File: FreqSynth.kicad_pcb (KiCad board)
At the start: 4 copper layers, 79 x 50 mm, 118 parts, among them IC1 ATMEGA32U2, P1 CPL-CON-BARREL-2.1MM, P10 RESET, P2 RF1, P3 RF2P, P4 RF2N, P5 USB_MINI_B, P6 CONN_01X06, P7 REF_IN, P8 VTEST, P9 PWRSEL, U1 MAX2870, U2 TS5A3159, U5 CPL-REG-LIN-3.3V-0.15A, U6 SKY13322-375LF, U7 SKY13322-375LF, U8 TRF37A75, U9 PE43711, X1 25MHz ±5ppm 3.3V 33mA, X2 8MHz 18PF 50ppm

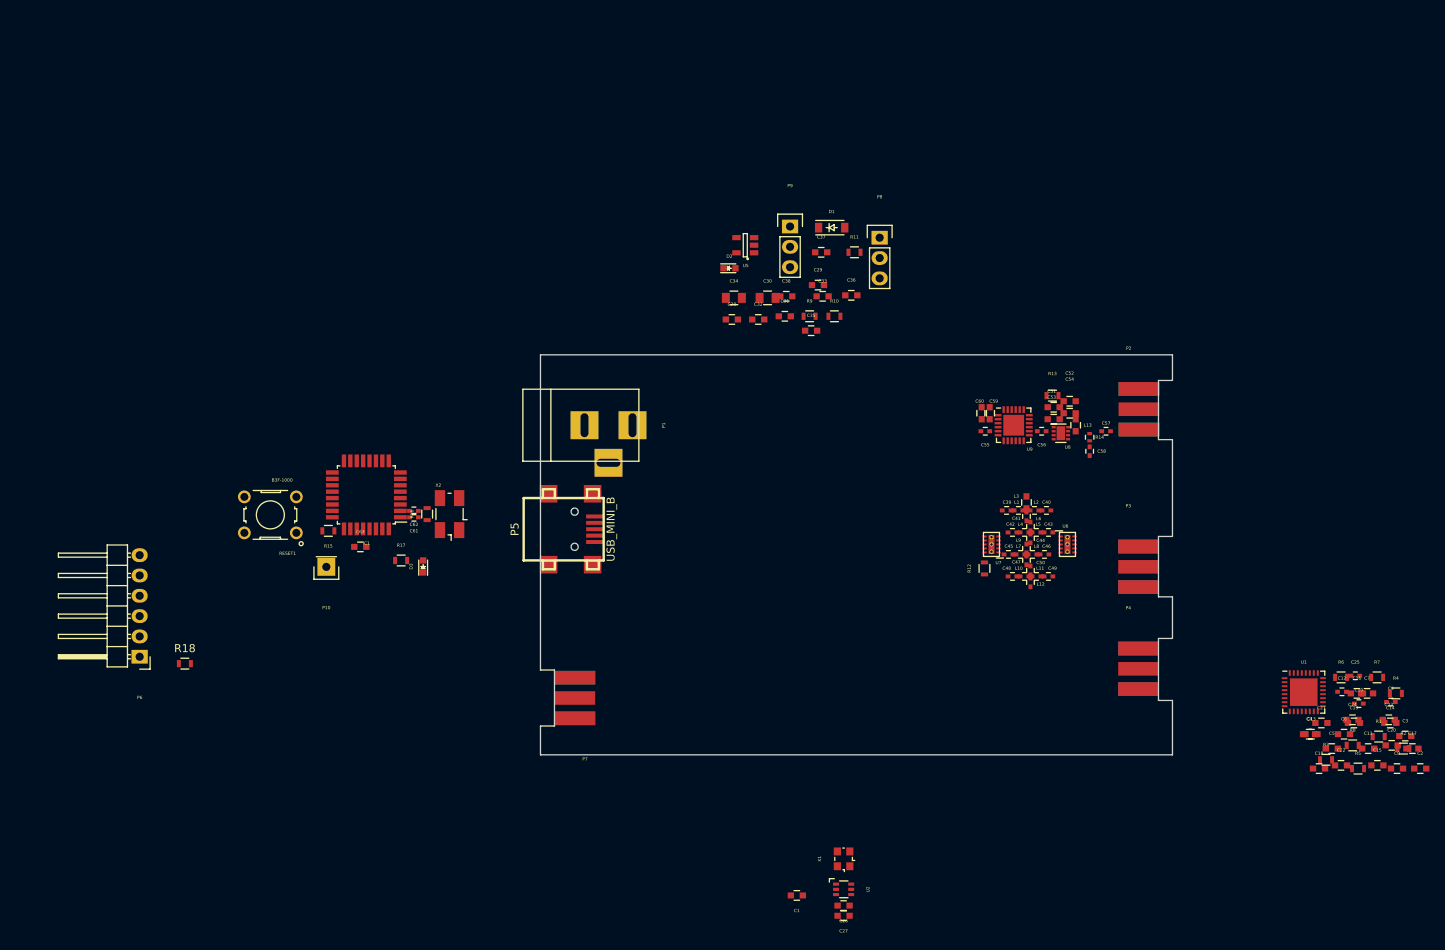
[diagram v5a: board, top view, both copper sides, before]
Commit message: Added power meter, swaped some pins, and routetd most of the RF
Signed-off-by: Martin Berglund <LeastSignificantBit@users.noreply.github.com>
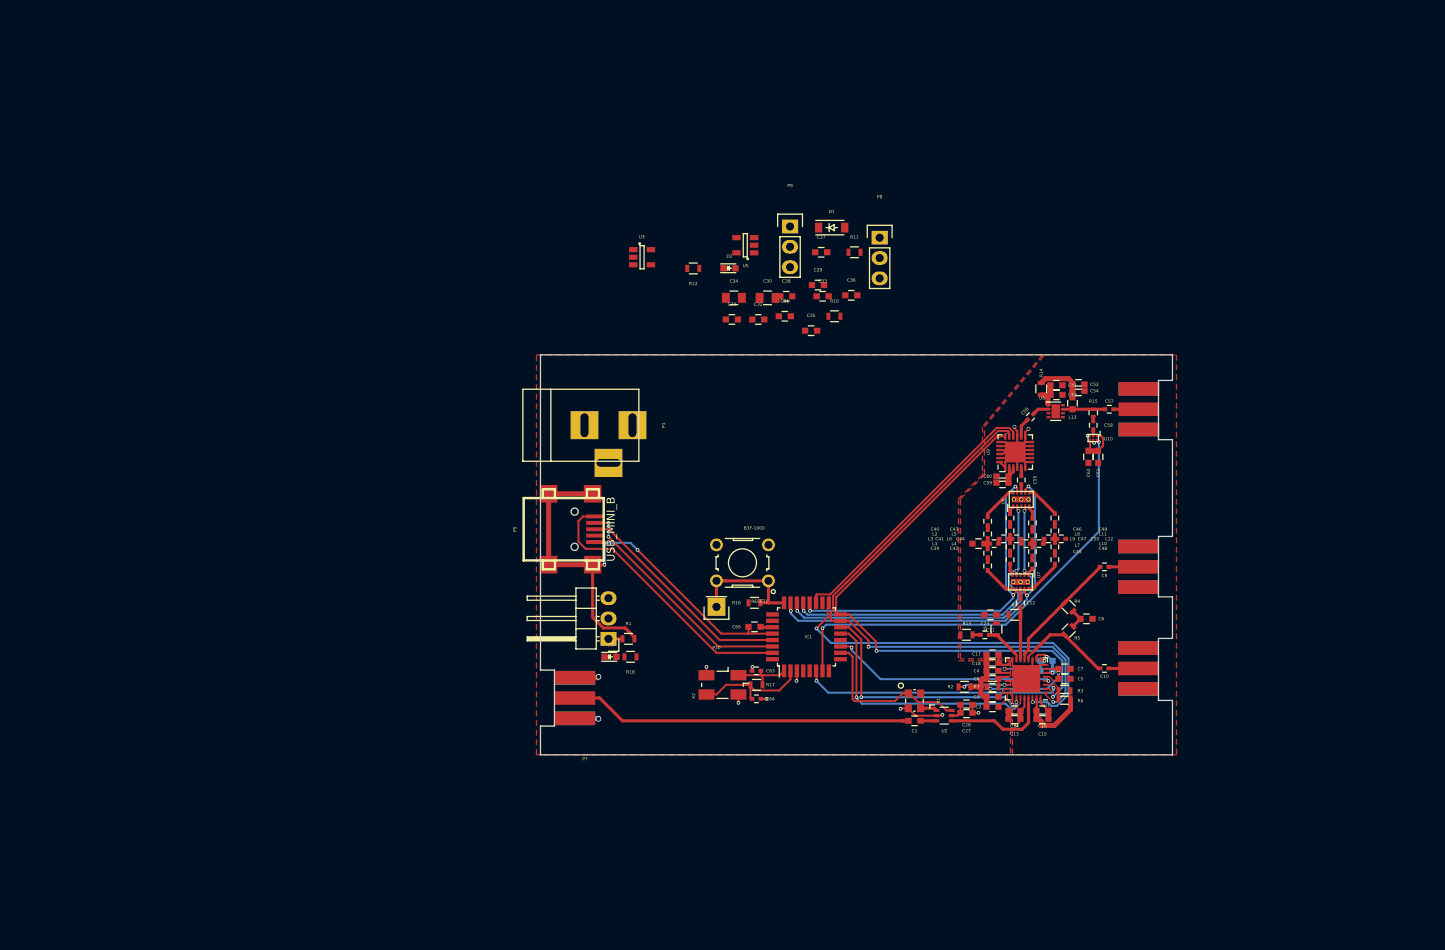
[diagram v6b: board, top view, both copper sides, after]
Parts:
- removed the C19 at (202.2, 146.0)
- removed C22, C24: 100pF, Capacitors_SMD:C_0603
- removed the C23 at (206.5, 145.6)
- added C64: 22p, Capacitors_SMD:C_0402, F.Cu at (127.5, 143.0)
- added C65: 1µF, Capacitors_SMD:C_0603, F.Cu at (127.2, 134.0)
- added U10: LMH2110, FreqSynth:WFBGA-6, F.Cu at (169.6, 110.4)
- added U3: CPL-REG-LIN-3.3V-1A, TO_SOT_Packages_SMD:SOT-23-5, F.Cu at (113.2, 87.8)
- C19: renamed from C21; moved to B.Cu
- C20: moved to B.Cu
- C61: value 22p -> 10nF; footprint Capacitors_SMD:C_0402 -> Capacitors_SMD:C_0603
- C62: value 22p -> 100pF; footprint Capacitors_SMD:C_0402 -> Capacitors_SMD:C_0603
- C63: value 1µF -> 22p; footprint Capacitors_SMD:C_0603 -> Capacitors_SMD:C_0402
- P6: value CONN_01X06 -> CONN_01X03; footprint Pin_Headers:Pin_Header_Angled_1x06 -> Pin_Headers:Pin_Header_Angled_1x03
- R1: value 5.1k -> 0R
- R11: value 33R -> 0R
- R12: value 49.9R -> 33R
- R13: value 1.8R -> 49.9R
- R14: value 100R -> 1.8R; footprint Resistors_SMD:R_0402 -> Resistors_SMD:R_0603
- R15: value 10k -> 100R; footprint Resistors_SMD:R_0603 -> Resistors_SMD:R_0402
- R16: value 1M -> 10k
- R17: value 33R -> 1M
- R18: value 0R -> 33R
- R2: value 30.1R -> 5.1k
- R3: value 49.9R -> 30.1R
- R5: value 90.9R -> 49.9R
- R6: value 240R -> 90.9R
- R7: value 49.9R -> 240R
- R9: value 0R -> 49.9R
- X1: footprint Crystals:Crystal_SMD_2520_4Pads -> FreqSynth:OSC_2.7x2.4mm
- moved R15 96.7 mm to (169.6, 107.2), turned to 270 degrees
- moved R1 94.6 mm to (111.5, 135.5)
- moved C61 85.8 mm to (170.2, 112.8), turned to 270 degrees
- moved C62 84.6 mm to (169.0, 112.8), turned to 270 degrees
- moved RESET1 59.3 mm to (125.8, 126.0)
- moved P6 58.6 mm to (109.0, 135.5)
- moved IC1 57.8 mm to (133.8, 135.2), turned to 90 degrees
- moved R18 55.7 mm to (111.8, 137.8), turned to 180 degrees
- moved R2 55.4 mm to (153.5, 141.5), turned to 180 degrees
- moved C2 54.0 mm to (157.0, 144.0)
- moved C17 53.8 mm to (157.0, 137.5), turned to 180 degrees
- moved R12 52.3 mm to (119.6, 89.2), turned to 180 degrees
- moved C63 51.9 mm to (127.5, 139.5)
- moved C3 51.8 mm to (157.0, 142.8)
- moved C8 51.8 mm to (157.0, 140.5)
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- renumbered C25 to C23
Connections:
- C10 pad 1: /PLL/RF_BALANCED- -> /PLL/RF_BALANCED+
- C10 pad 2: /PLL/RFB_N -> /PLL/RFA_P
- C11 pad 1: /Amplifier/VCC_AMP -> /Amplifier/3V3
- C12 pad 2: /PLL/RFA_P -> /PLL/RFB_P
- C17 pad 1: /Amplifier/VCC_AMP -> /Amplifier/3V3
- C18 pad 1: /Amplifier/VCC_AMP -> /Amplifier/3V3
- C20 pad 1: /Amplifier/VCC_AMP -> /PLL/VCC_PLL
- C20 pad 2: Earth -> GNDD
- C23 pad 2: /PLL/RFA_N -> /PLL/RFB_N
- C32 pad 1: /Amplifier/VCC_AMP -> /Amplifier/3V3
- C33 pad 1: /Amplifier/VCC_AMP -> /Amplifier/3V3
- C51 pad 2: /Amplifier/VCC_AMP -> /Amplifier/3V3
- C53 pad 2: /Amplifier/VCC_AMP -> /Amplifier/3V3
- C6 pad 1: /Amplifier/VCC_AMP -> /Amplifier/3V3
- C61 pad 1: GNDD -> /Amplifier/3V3
- C61 pad 2: Net-(C61-Pad2) -> Earth
- C62 pad 1: GNDD -> /Amplifier/3V3
- C62 pad 2: Net-(C62-Pad2) -> Earth
- C63 pad 1: Net-(C63-Pad1) -> GNDD
- C63 pad 2: GNDPWR -> Net-(C63-Pad2)
- C9 pad 1: /PLL/RF_BALANCED+ -> /PLL/RF_BALANCED-
- C9 pad 2: /PLL/RFB_P -> /PLL/RFA_N
- IC1 pad 1: Net-(C61-Pad2) -> Net-(C63-Pad2)
- IC1 pad 10: /FILT1 -> /MCU/EXT_CLK_EN
- IC1 pad 11: /FILT2 -> /MCU/CE_PLL
- IC1 pad 12: /FILT3 -> Net-(IC1-Pad12)
- IC1 pad 13: /FILT4 -> /MCU/EN_PLL
- IC1 pad 14: /MCU/SS_EXT -> /MCU/LD_PLL
- IC1 pad 19: Net-(IC1-Pad19) -> /Amplifier/ATTEN_CS
- IC1 pad 2: Net-(C62-Pad2) -> Net-(C64-Pad2)
- IC1 pad 20: Net-(IC1-Pad20) -> /FILT1
- IC1 pad 21: Net-(IC1-Pad21) -> /FILT4
- IC1 pad 22: Net-(D3-Pad1) -> /FILT3
- IC1 pad 23: /MCU/EXT_CLK_EN -> /FILT2
- IC1 pad 26: /Amplifier/ATTEN_CS -> Net-(IC1-Pad26)
- IC1 pad 27: Net-(C63-Pad1) -> Net-(C65-Pad1)
- IC1 pad 5: Net-(IC1-Pad5) -> Net-(D3-Pad1)
- IC1 pad 7: /MCU/CE_PLL -> /MCU/ADC1
- IC1 pad 8: /MCU/LD_PLL -> /MCU/TX
- IC1 pad 9: /MCU/EN_PLL -> /MCU/RX
- P6 pad 2: Net-(P6-Pad2) -> /MCU/RX
- P6 pad 3: Net-(P6-Pad3) -> /MCU/TX
- P8 pad 2: /Amplifier/VCC_AMP -> /Amplifier/3V3
- R1 pad 1: Earth -> Net-(P6-Pad1)
- R1 pad 2: Net-(R1-Pad2) -> GNDPWR
- R10 pad 1: Earth -> GNDD
- R11 pad 1: VCC -> Earth
- R11 pad 2: Net-(D2-Pad2) -> GNDPWR
- R12 pad 1: /PLL/RF- -> VCC
- R12 pad 2: Earth -> Net-(D2-Pad2)
- R13 pad 1: /Amplifier/VCC_AMP -> /PLL/RF-
- R13 pad 2: Net-(C52-Pad1) -> Earth
- R14 pad 1: Net-(C57-Pad2) -> /Amplifier/3V3
- R14 pad 2: Net-(C58-Pad2) -> Net-(C52-Pad1)
- R15 pad 1: VCC -> Net-(C57-Pad2)
- R15 pad 2: Net-(IC1-Pad24) -> Net-(C58-Pad2)
- R16 pad 1: Net-(C61-Pad2) -> VCC
- R16 pad 2: Net-(C62-Pad2) -> Net-(IC1-Pad24)
- R17 pad 1: VCC -> Net-(C63-Pad2)
- R17 pad 2: Net-(D3-Pad2) -> Net-(C64-Pad2)
- R18 pad 1: Net-(P6-Pad1) -> VCC
- R18 pad 2: GNDPWR -> Net-(D3-Pad2)
- R2 pad 1: Net-(C5-Pad2) -> Earth
- R3 pad 1: /Amplifier/VCC_AMP -> Net-(C5-Pad2)
- R3 pad 2: /PLL/RFB_P -> Net-(R3-Pad2)
- R4 pad 1: /Amplifier/VCC_AMP -> /Amplifier/3V3
- R4 pad 2: /PLL/RFB_N -> /PLL/RFA_N
- R5 pad 1: GNDD -> /Amplifier/3V3
- R5 pad 2: Net-(R2-Pad2) -> /PLL/RFA_P
- R6 pad 1: /PLL/TUNE -> GNDD
- R6 pad 2: Net-(C5-Pad1) -> Net-(R3-Pad2)
- R7 pad 1: /Amplifier/VCC_AMP -> /PLL/TUNE
- R7 pad 2: /PLL/RFA_P -> Net-(C5-Pad1)
- R8 pad 1: /Amplifier/VCC_AMP -> /Amplifier/3V3
- R8 pad 2: /PLL/RFA_N -> /PLL/RFB_P
- R9 pad 1: GNDD -> /Amplifier/3V3
- R9 pad 2: GNDPWR -> /PLL/RFB_N
- U1 pad 16: /Amplifier/VCC_AMP -> /Amplifier/3V3
- U1 pad 17: /Amplifier/VCC_AMP -> /Amplifier/3V3
- U1 pad 22: Net-(R1-Pad2) -> Net-(R2-Pad2)
- U1 pad 5: Net-(R2-Pad2) -> Net-(R3-Pad2)
- U8 pad 1: /Amplifier/VCC_AMP -> /Amplifier/3V3
- X2 pad 1: Net-(C61-Pad2) -> Net-(C63-Pad2)
- X2 pad 2: Net-(C62-Pad2) -> Net-(C64-Pad2)
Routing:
- net /SCK: track 0.00 -> 73.8 mm, vias 0 -> 2
- net /MOSI: track 0.00 -> 69.6 mm, vias 0 -> 2
- net GNDPWR: track 0.00 -> 64.9 mm, vias 0 -> 3
- net /MCU/ADC1: track 0.00 -> 56.5 mm, vias 0 -> 2
- net /FILT2: track 0.00 -> 49.2 mm, vias 0 -> 3
- net /MISO: track 0.00 -> 47.2 mm, vias 0 -> 2
- net /FILT3: track 0.00 -> 43.8 mm, vias 0 -> 3
- net /FILT1: track 0.00 -> 43.7 mm, vias 0 -> 3
- net Net-(C1-Pad2): track 0.00 -> 43.7 mm
- net /FILT4: track 0.00 -> 42.2 mm, vias 0 -> 3
- net Earth: track 0.00 -> 42.2 mm, vias 0 -> 4
- net GNDD: track 0.00 -> 38.4 mm, vias 0 -> 12
- net /Amplifier/ATTEN_CS: track 0.00 -> 35.0 mm
- net /Power/VUSB: track 0.00 -> 34.9 mm
- net /MCU/CS_PLL: track 0.00 -> 33.1 mm, vias 0 -> 2
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- added copper zone on F.Cu, net Earth
- added copper zone on In1.Cu, net Earth
- added copper zone on F.Cu, net GNDD
- added copper zone on In1.Cu, net GNDD
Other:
- net class 50Ohm added: clearance 0.127, trace_width 0.3937, via_dia 0.4572, via_drill 0.254

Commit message: Starting to clean up
Signed-off-by: Martin Berglund <LeastSignificantBit@users.noreply.github.com>
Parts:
- removed the C31 at (131.0, 95.2)
- removed the P8 at (142.9, 85.4)
- removed P9: PWRSEL, Pin_Headers:Pin_Header_Straight_1x03
- added C28: 1µF, Capacitors_SMD:C_0603, F.Cu at (92.8, 78.9)
- added C29: 100nF, Capacitors_SMD:C_0603, F.Cu at (88.6, 78.9)
- added C63: 10nF, Capacitors_SMD:C_0603, F.Cu at (134.5, 142.5)
- added C64: 100pF, Capacitors_SMD:C_0603, F.Cu at (133.0, 142.5)
- added TH1: 750mA working 1.5A trip, FreqSynth:SMD_THERMISTOR, F.Cu at (117.7, 106.2)
- added U5: CPL-REG-LIN-3.3V-0.15A, TO_SOT_Packages_SMD:SOT-23-5, F.Cu at (96.5, 72.7)
- C30: value 10µF -> 10nF; footprint Capacitors_SMD:C_0805 -> Capacitors_SMD:C_0603
- moved C30 35.3 mm to (96.4, 78.9)
- renumbered C23 to C21, C26 to C22, C27 to C23, C28 to C24, C29 to C25, C32 to C26, C33 to C27, C34 to C31, C35 to C32, C36 to C33, C37 to C34, C38 to C35, C39 to C36, C40 to C37, C41 to C38, C42 to C39, C43 to C40, C44 to C41, C45 to C42, C46 to C43, C47 to C44, C48 to C45, C49 to C46, C50 to C47, C51 to C48, C52 to C49, C53 to C50, C54 to C51, C55 to C52, C56 to C53, C57 to C54, C58 to C55, C59 to C56, C60 to C57, C61 to C58, C62 to C59, C63 to C60, C64 to C61, C65 to C62, P10 to P8, R12 to R10, R10 to R11, R11 to R12, R18 to R17, R17 to R18, U9 to U10, U10 to U11, U5 to U6, U6 to U7, U7 to U8, U8 to U9
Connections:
- C11 pad 1: /Amplifier/3V3 -> /PLL/VCC_RF
- C13 pad 1: VCC -> /MCU/VCC_D
- C14 pad 1: VCC -> /MCU/VCC_D
- C15 pad 1: VCC -> /MCU/VCC_D
- C16 pad 1: VCC -> /MCU/VCC_D
- C17 pad 1: /Amplifier/3V3 -> /PLL/VCC_RF
- C18 pad 1: /Amplifier/3V3 -> /PLL/VCC_RF
- C22 pad 1: VCC -> /3v3
- C23 pad 1: VCC -> /3v3
- C24 pad 1: VCC -> /MCU/VCC_D
- C25 pad 1: VCC -> /MCU/VCC_D
- C26 pad 1: /Amplifier/3V3 -> /PLL/VCC_RF
- C26 pad 2: Earth -> Net-(C26-Pad2)
- C27 pad 1: /Amplifier/3V3 -> /PLL/VCC_RF
- C27 pad 2: Earth -> Net-(C26-Pad2)
- C30 pad 1: /Power/VUSB -> Net-(C30-Pad1)
- C30 pad 2: GNDPWR -> GNDD
- C48 pad 2: /Amplifier/3V3 -> /5V5
- C50 pad 2: /Amplifier/3V3 -> /5V5
- C56 pad 1: /Amplifier/3V3 -> /3v3
- C57 pad 1: /Amplifier/3V3 -> /3v3
- C58 pad 1: /Amplifier/3V3 -> /3v3
- C59 pad 1: /Amplifier/3V3 -> /3v3
- C6 pad 1: /Amplifier/3V3 -> /PLL/VCC_RF
- IC1 pad 31: /Power/VUSB -> /MCU/V_USB
- IC1 pad 32: VCC -> /MCU/VCC_D
- IC1 pad 4: VCC -> /MCU/VCC_D
- P1 pad 1: /Power/VIN -> Net-(P1-Pad1)
- P5 pad 1: /Power/VUSB -> /MCU/V_USB
- R10 pad 1: VCC -> /MCU/VCC_D
- R14 pad 1: /Amplifier/3V3 -> /5V5
- R16 pad 1: VCC -> /MCU/VCC_D
- R17 pad 1: VCC -> /MCU/VCC_D
- R4 pad 1: /Amplifier/3V3 -> /PLL/VCC_RF
- R5 pad 1: /Amplifier/3V3 -> /PLL/VCC_RF
- R8 pad 1: /Amplifier/3V3 -> /PLL/VCC_RF
- R9 pad 1: /Amplifier/3V3 -> /PLL/VCC_RF
- U1 pad 16: /Amplifier/3V3 -> /PLL/VCC_RF
- U1 pad 17: /Amplifier/3V3 -> /PLL/VCC_RF
- U1 pad 28: VCC -> /MCU/VCC_D
- U1 pad 32: VCC -> /MCU/VCC_D
- U10 pad 2: /Amplifier/3V3 -> /3v3
- U10 pad 3: /Amplifier/3V3 -> /3v3
- U11 pad A1: /Amplifier/3V3 -> /3v3
- U11 pad C2: /Amplifier/3V3 -> /3v3
- U2 pad 5: VCC -> /3v3
- U3 pad 1: Net-(P9-Pad2) -> /Power/VIN
- U3 pad 3: VCC -> /MCU/VCC_D
- U6 pad 1: Net-(P9-Pad2) -> Net-(U6-Pad1)
- U6 pad 3: Net-(P9-Pad2) -> Net-(U6-Pad1)
- U9 pad 1: /Amplifier/3V3 -> /5V5
- X1 pad 4: VCC -> /3v3
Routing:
- net /MCU/VCC_D: track 0.00 -> 50.7 mm, vias 0 -> 5
- net /Power/VUSB: track 34.9 -> 0.00 mm
- net /MCU/V_USB: track 0.00 -> 34.9 mm
- net /MCU/RX: track 0.00 -> 32.3 mm, vias 0 -> 2
- net /MCU/TX: track 0.00 -> 31.9 mm, vias 0 -> 2
- net /Amplifier/3V3: track 18.2 -> 0.00 mm
- net /3v3: track 0.00 -> 11.1 mm
- net VCC: track 9.02 -> 0.00 mm, vias 1 -> 0
- net /PLL/VCC_RF: track 0.00 -> 5.78 mm
- net /5V5: track 0.00 -> 3.64 mm

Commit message: Board layout almost done
Signed-off-by: Martin Berglund <LeastSignificantBit@users.noreply.github.com>
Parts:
- removed the C26 at (127.7, 95.6)
- removed the D2 at (124.1, 89.2)
- added ?: , FreqSynth:VIA, F.Cu at (161.0, 121.6)
- added C25: 22µF 16V, Capacitors_SMD:C_0805, F.Cu at (118.8, 111.5)
- added C32: 1µF, Capacitors_SMD:C_0603, F.Cu at (110.5, 116.8)
- added D3: CPL-LED-0603-GREEN, LEDs:LED_0603, F.Cu at (104.0, 128.5)
- added L1: Ferrite, FreqSynth:L_0603, F.Cu at (161.0, 104.5)
- added L2: Ferrite, FreqSynth:L_0603, F.Cu at (157.0, 145.5)
- added L3: Ferrite, FreqSynth:L_0603, F.Cu at (167.8, 112.8)
- added L4: Ferrite, FreqSynth:L_0603, F.Cu at (156.8, 131.5)
- added L5: Ferrite, FreqSynth:L_0603, F.Cu at (165.4, 138.2)
- added L6: Ferrite, FreqSynth:L_0603, F.Cu at (137.0, 141.5)
- added L7: Ferrite, FreqSynth:L_0603, F.Cu at (145.5, 140.0)
- added L8: 6.8µH 2.5A, FreqSynth:NRS5030T6R8MMGJ, F.Cu at (114.0, 117.5)
- added R13: 11.3k, Resistors_SMD:R_0603, F.Cu at (124.8, 116.8)
- added R20: 33R, Resistors_SMD:R_0603, F.Cu at (110.5, 138.0)
- added SG1: StarGND, FreqSynth:NetTie-II_Connected_SMD, B.Cu at (121.2, 112.8)
- added U4: AP65101, TO_SOT_Packages_SMD:SOT-23-6, F.Cu at (118.5, 116.8)
- C27, C29, C34: value 100nF -> 1µF
- C30, C35: value 10nF -> 1µF
- C31: value 10µF -> 1µF; footprint Capacitors_SMD:C_0805 -> Capacitors_SMD:C_0603
- C33: value 1µF -> 22µF 16V; footprint Capacitors_SMD:C_0603 -> Capacitors_SMD:C_0805
- R10: value 33R -> 45.3k
- R11: value 0R -> 59k
- R12: value 0R -> 100k
- U3: value CPL-REG-LIN-3.3V-1A -> TLV7113333DDSET; footprint TO_SOT_Packages_SMD:SOT-23-5 -> FreqSynth:WSON-6
- U5: value CPL-REG-LIN-3.3V-0.15A -> TLV7113333DDSET; footprint TO_SOT_Packages_SMD:SOT-23-5 -> FreqSynth:WSON-6
- U6: value CPL-REG-LIN-3.3V-0.15A -> RT9069-50GB
- U9: footprint Housings_DFN_QFN:DFN-8-1EP_2x2mm_Pitch0.5mm -> FreqSynth:DFN-8-1EP_2x2mm_Pitch0.5mm
- moved C28 63.5 mm to (138.0, 123.5), turned to 270 degrees
- moved C29 61.6 mm to (138.0, 115.8), turned to 270 degrees
- moved U5 59.6 mm to (136.2, 117.2), turned to 270 degrees
- moved C30 52.8 mm to (134.2, 115.8), turned to 90 degrees
- moved U3 41.7 mm to (136.2, 122.5), turned to 270 degrees
- moved C34 36.7 mm to (119.8, 120.2), turned to 270 degrees
- moved C33 35.2 mm to (118.0, 120.5), turned to 270 degrees
- moved R12 34.9 mm to (121.2, 116.8), turned to 270 degrees
- moved D1 31.6 mm to (118.1, 109.5), turned to 180 degrees
- moved R10 31.1 mm to (121.2, 120.2), turned to 90 degrees
- moved C24 28.8 mm to (138.0, 121.0), turned to 270 degrees
- moved C31 28.7 mm to (138.0, 118.2), turned to 270 degrees
- moved C27 28.4 mm to (134.2, 121.0), turned to 90 degrees
- moved R11 25.8 mm to (123.0, 116.8), turned to 90 degrees
- moved C26 22.5 mm to (118.8, 113.2), turned to 180 degrees
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- renumbered C32 to C26, C25 to C36, C36 to C37, C37 to C38, C38 to C39, C39 to C40, C40 to C41, C41 to C42, C42 to C43, C43 to C44, C44 to C45, C45 to C46, C46 to C47, C47 to C48, C48 to C49, C49 to C50, C50 to C51, C51 to C52, C52 to C53, C53 to C54, C54 to C55, C55 to C56, C56 to C57, C57 to C58, C58 to C59, C59 to C60, C60 to C61, C61 to C62, C62 to C63, C63 to C64, C64 to C65, D3 to D2, L2 to L10, L3 to L11, L4 to L12, L5 to L13, L6 to L14, L7 to L15, L8 to L16, L9 to L17, L10 to L18, L11 to L19, L12 to L20, L13 to L21, L1 to L9, R13 to R14, R14 to R15, R15 to R16, R16 to R17, R17 to R18, R18 to R19
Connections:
- C13 pad 1: /MCU/VCC_D -> /PLL/VCC_D
- C14 pad 1: /MCU/VCC_D -> /PLL/VCC_D
- C15 pad 1: /MCU/VCC_D -> /PLL/VCC_D
- C16 pad 1: /MCU/VCC_D -> /PLL/VCC_D
- C22 pad 1: /3v3 -> /Clock/3V3
- C23 pad 1: /3v3 -> /Clock/3V3
- C24 pad 1: /MCU/VCC_D -> GNDD
- C24 pad 2: GNDD -> /Power/VCC_D
- C27 pad 1: /PLL/VCC_RF -> /Power/4V0
- C27 pad 2: Net-(C26-Pad2) -> GNDD
- C28 pad 1: /3v3 -> /Power/VCC_PLL
- C28 pad 2: GNDD -> Earth
- C29 pad 1: /3v3 -> Earth
- C29 pad 2: GNDD -> /3v3
- C30 pad 1: Net-(C30-Pad1) -> /Power/4V0
- C30 pad 2: GNDD -> Earth
- C31 pad 1: /Power/VIN -> /Power/VCC_RF
- C31 pad 2: GNDPWR -> Earth
- C33 pad 1: /PLL/VCC_PLL -> /Power/4V0
- C33 pad 2: GNDD -> GNDPWR
- C34 pad 1: /PLL/VCC_PLL -> /Power/4V0
- C34 pad 2: GNDD -> GNDPWR
- C35 pad 1: Net-(C35-Pad1) -> /5V5
- C35 pad 2: GNDD -> Earth
- C36 pad 1: /MCU/VCC_D -> /Power/VIN
- C36 pad 2: GNDD -> Earth
- C49 pad 2: /5V5 -> /Amplifier/VCC_AMP
- C51 pad 2: /5V5 -> /Amplifier/VCC_AMP
- C57 pad 1: /3v3 -> /Amplifier/3V3
- C58 pad 1: /3v3 -> /Amplifier/3V3
- C59 pad 1: /3v3 -> /Amplifier/3V3
- C60 pad 1: /3v3 -> /Amplifier/3V3
- R10 pad 1: /MCU/VCC_D -> Net-(R10-Pad1)
- R10 pad 2: Net-(D2-Pad2) (its old number) -> /Power/4V0
- R11 pad 1: GNDD -> Net-(R10-Pad1)
- R11 pad 2: GNDPWR -> Net-(R11-Pad2)
- R12 pad 1: Earth -> /Power/VIN
- R12 pad 2: GNDPWR -> Net-(R12-Pad2)
- R15 pad 1: /5V5 -> /Amplifier/VCC_AMP
- U1 pad 28: /MCU/VCC_D -> /PLL/VCC_D
- U1 pad 32: /MCU/VCC_D -> /PLL/VCC_D
- U10 pad 2: /3v3 -> /Amplifier/3V3
- U10 pad 3: /3v3 -> /Amplifier/3V3
- U11 pad A1: /3v3 -> /Amplifier/3V3
- U11 pad C2: /3v3 -> /Amplifier/3V3
- U2 pad 5: /3v3 -> /Clock/3V3
- U3 pad 1: /Power/VIN -> /Power/4V0
- U3 pad 2: GNDD -> /Power/4V0
- U3 pad 3: /MCU/VCC_D -> /Power/4V0
- U3 pad 4: (no net) -> GNDD
- U3 pad 5: (no net) -> /Power/VCC_PLL
- U5 pad 1: /Power/VIN -> /Power/4V0
- U5 pad 2: GNDD -> /Power/4V0
- U5 pad 3: /Power/VIN -> /Power/4V0
- U5 pad 4: Net-(C30-Pad1) -> Earth
- U5 pad 5: /3v3 -> /Power/VCC_RF
- U6 pad 1: Net-(U6-Pad1) -> /Power/VIN
- U6 pad 2: GNDD -> Earth
- U6 pad 3: Net-(U6-Pad1) -> Earth
- U6 pad 4: Net-(C35-Pad1) -> /Power/VIN
- U6 pad 5: /PLL/VCC_PLL -> /5V5
- U9 pad 1: /5V5 -> /Amplifier/VCC_AMP
- X1 pad 4: /3v3 -> /Clock/3V3
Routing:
- net Earth: track 42.2 -> 170.9 mm, vias 4 -> 20
- net GNDPWR: track 64.9 -> 127.0 mm, vias 3 -> 9
- net /Power/VCC_D: track 0.00 -> 60.9 mm, vias 0 -> 6
- net /3v3: track 11.1 -> 61.2 mm, vias 0 -> 8
- net /Power/VCC_PLL: track 0.00 -> 40.7 mm, vias 0 -> 3
- net GNDD: track 38.4 -> 73.4 mm, vias 12 -> 26
- net Net-(D2-Pad1): track 0.00 -> 34.2 mm, vias 0 -> 2
- net /Power/4V0: track 0.00 -> 31.9 mm
- net /5V5: track 3.64 -> 34.5 mm
- net /Power/VCC_RF: track 0.00 -> 27.3 mm, vias 0 -> 4
- net /PLL/VCC_RF: track 5.78 -> 31.2 mm, vias 0 -> 4
- net /Amplifier/3V3: track 0.00 -> 23.7 mm, vias 0 -> 3
- net /Power/VIN: track 0.00 -> 20.3 mm
- net /PLL/VCC_D: track 0.00 -> 15.0 mm, vias 0 -> 2
- net Net-(D3-Pad2): track 0.00 -> 11.9 mm
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- added copper zone on B.Cu, net Earth
- added copper zone on In2.Cu, net Earth
- added copper zone on B.Cu, net GNDD
- added copper zone on In2.Cu, net GNDD
- added copper zone on B.Cu, net GNDPWR
- added copper zone on F.Cu, net GNDPWR
- added copper zone on In1.Cu, net GNDPWR
- added copper zone on In2.Cu, net GNDPWR
